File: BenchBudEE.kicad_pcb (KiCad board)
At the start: 2 copper layers, 0 parts

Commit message: 4.18 Initial board layout and design rules mods
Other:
- board outline added: 165.1 x 63.5 mm
- copper layers 2 -> 4
- rule trace_min: 0.254 -> 0.1524
- rule via_min_drill: 0.508 -> 0.3302
- rule via_min_size: 0.889 -> 0.508
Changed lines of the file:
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@@
-(kicad_pcb (version 3) (host pcbnew "(2013-mar-13)-testing")
+(kicad_pcb (version 3) (host pcbnew "(2013-07-07 BZR 4022)-stable")
   (general
     (links 0)
@@
     (area 0 0 0 0)
     (thickness 1.6)
-    (drawings 0)
+    (drawings 4)
     (tracks 0)
     (zones 0)
@@
   (layers
     (15 F.Cu signal)
+    (2 PWR power)
+    (1 GND power)
     (0 B.Cu signal)
     (16 B.Adhes user)
@@
     (22 B.Mask user)
     (23 F.Mask user)
-    (24 Dwgs.User user)
-    (25 Cmts.User user)
-    (26 Eco1.User user)
-    (27 Eco2.User user)
     (28 Edge.Cuts user)
   )
   (setup
     (last_trace_width 0.254)
+    (user_trace_width 0.1524)
     (trace_clearance 0.254)
     (zone_clearance 0.508)
     (zone_45_only no)
-    (trace_min 0.254)
+    (trace_min 0.1524)
     (segment_width 0.2)
     (edge_width 0.1)
     (via_size 0.889)
     (via_drill 0.635)
-    (via_min_size 0.889)
-    (via_min_drill 0.508)
+    (via_min_size 0.508)
+    (via_min_drill 0.3302)
+    (user_via 0.508 0.3302)
     (uvia_size 0.508)
     (uvia_drill 0.127)
     (uvias_allowed no)
-    (uvia_min_size 0.508)
+    (uvia_min_size 0.381)
     (uvia_min_drill 0.127)
     (pcb_text_width 0.3)
@@
     (pad_to_mask_clearance 0)
     (aux_axis_origin 0 0)
-    (visible_elements FFFFFF7F)
+    (visible_elements 7FFFFFFF)
     (pcbplotparams
       (layerselection 3178497)
@@
     (add_net "")
   )
+  (gr_line (start 67.31 67.183) (end 67.31 130.683) (angle 90) (layer Edge.Cuts) (width 0.1))
+  (gr_line (start 232.41 67.183) (end 67.31 67.183) (angle 90) (layer Edge.Cuts) (width 0.1))
+  (gr_line (start 232.41 130.683) (end 232.41 67.183) (angle 90) (layer Edge.Cuts) (width 0.1))
+  (gr_line (start 67.31 130.683) (end 232.41 130.683) (angle 90) (layer Edge.Cuts) (width 0.1))
 )

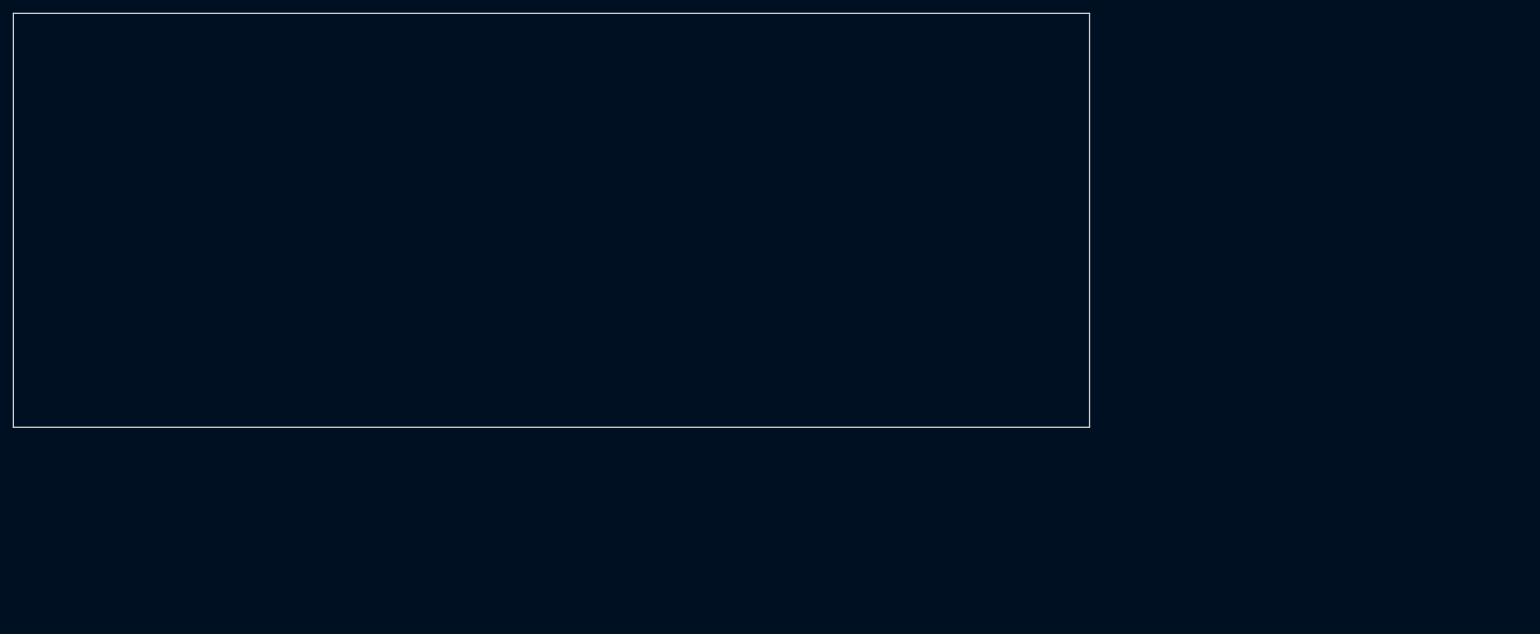
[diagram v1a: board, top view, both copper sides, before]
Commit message: 4.18 Video 2 Changed design rules for pin spacing
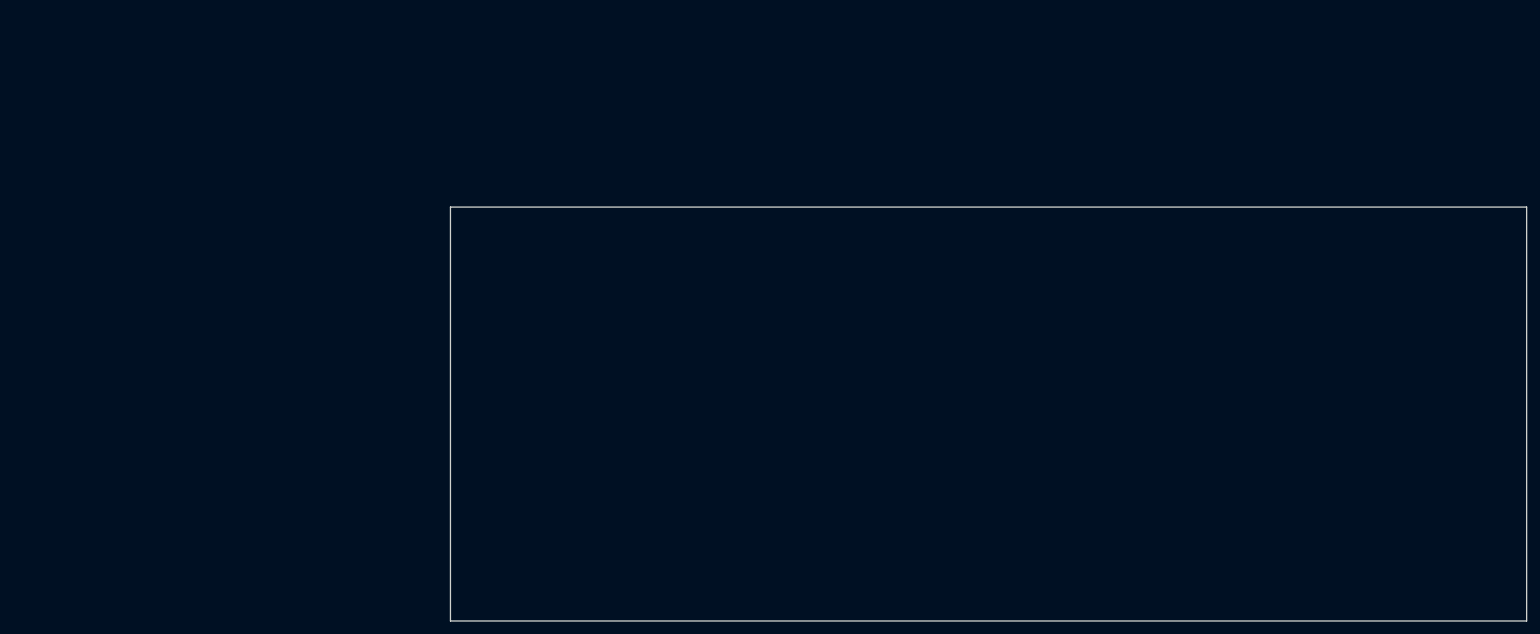
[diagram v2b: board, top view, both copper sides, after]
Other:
- rule pad_to_mask_clearance: 0 -> 0.254
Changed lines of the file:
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@@
     (links 0)
     (no_connects 0)
-    (area 0 0 0 0)
+    (area 104.597999 104.470999 269.798001 168.071001)
     (thickness 1.6)
     (drawings 4)
@@
     (nets 1)
   )
-  (page A4)
+  (page USLedger)
+  (title_block
+    (title BenchBudEE)
+    (rev A)
+    (company "Contextual Electronics")
+  )
   (layers
     (15 F.Cu signal)
@@
     (pad_size 1.5 1.5)
     (pad_drill 0.6)
-    (pad_to_mask_clearance 0)
+    (pad_to_mask_clearance 0.254)
+    (solder_mask_min_width 0.127)
     (aux_axis_origin 0 0)
     (visible_elements 7FFFFFFF)
@@
     (add_net "")
   )
-  (gr_line (start 67.31 67.183) (end 67.31 130.683) (angle 90) (layer Edge.Cuts) (width 0.1))
-  (gr_line (start 232.41 67.183) (end 67.31 67.183) (angle 90) (layer Edge.Cuts) (width 0.1))
-  (gr_line (start 232.41 130.683) (end 232.41 67.183) (angle 90) (layer Edge.Cuts) (width 0.1))
-  (gr_line (start 67.31 130.683) (end 232.41 130.683) (angle 90) (layer Edge.Cuts) (width 0.1))
+  (gr_line (start 134.366 96.901) (end 134.366 160.401) (angle 90) (layer Edge.Cuts) (width 0.1))
+  (gr_line (start 299.466 96.901) (end 134.366 96.901) (angle 90) (layer Edge.Cuts) (width 0.1))
+  (gr_line (start 299.466 160.401) (end 299.466 96.901) (angle 90) (layer Edge.Cuts) (width 0.1))
+  (gr_line (start 134.366 160.401) (end 299.466 160.401) (angle 90) (layer Edge.Cuts) (width 0.1))
 )

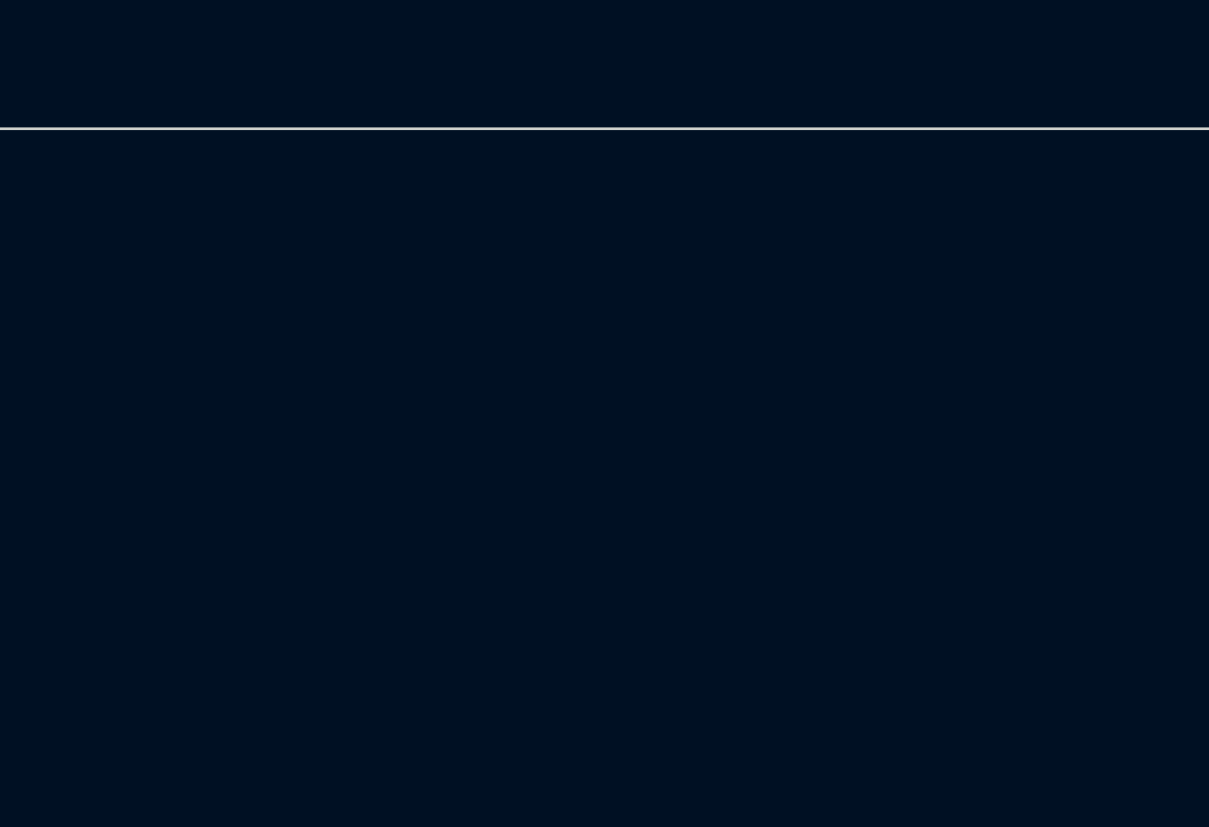
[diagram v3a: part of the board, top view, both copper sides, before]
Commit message: 5.3 Video 2/2 Associating and Placing the Relay Module
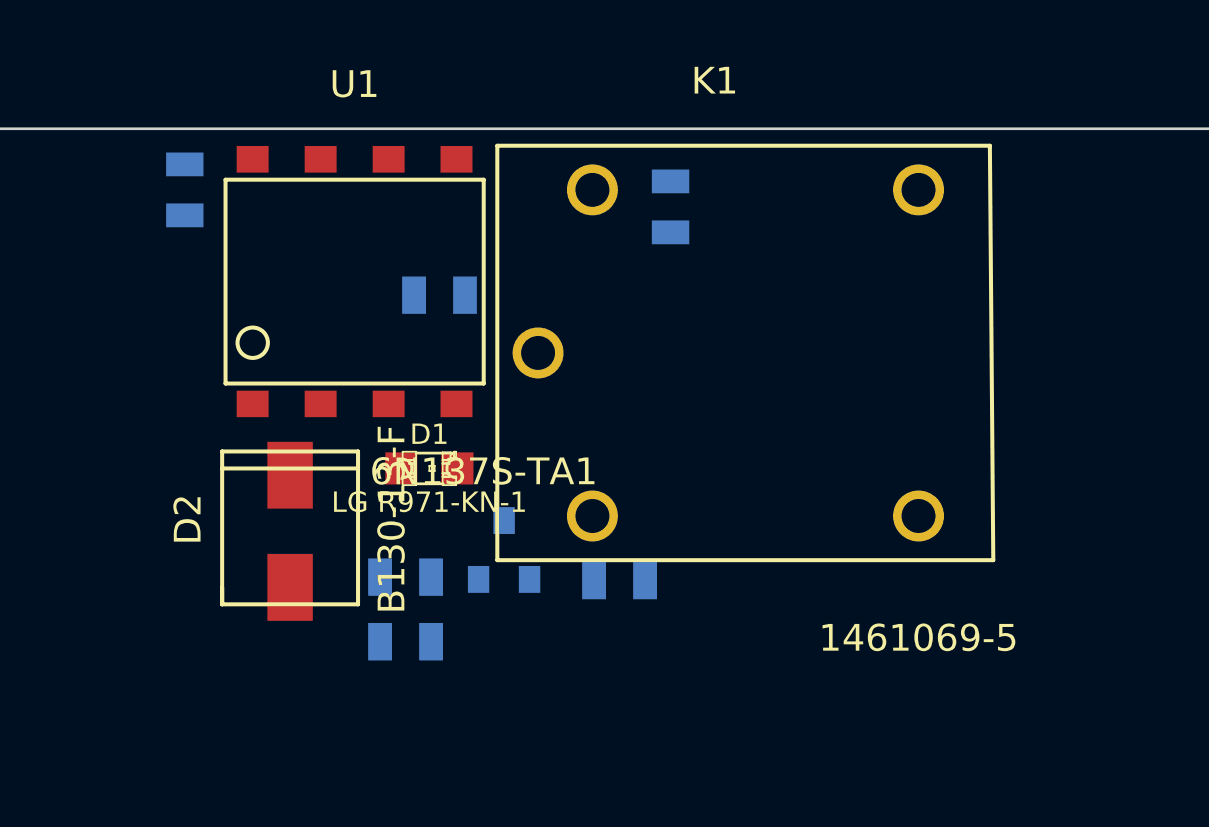
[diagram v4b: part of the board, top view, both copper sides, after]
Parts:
- added D1: LG R971-KN-1, LED-0805, F.Cu at (265.4, 109.6)
- added D2: B130-13-F, SMA, F.Cu at (260.2, 114.0)
- added K1: 1461069-5, TE-SPDT, F.Cu at (271.5, 111.4)
- added Q1: 1461069-5, SOT23, B.Cu at (268.2, 112.6)
- added R1: 500, SM0805, B.Cu at (256.3, 99.2)
- added R2: 200, SM0805, B.Cu at (264.5, 113.7)
- added R3: 100, SM0805, B.Cu at (272.5, 113.8)
- added R4: 0, SM0805, B.Cu at (265.8, 103.1)
- added R5: 0, SM0805, B.Cu at (264.5, 116.1)
- added R6: 0, SM0805, B.Cu at (274.4, 99.8)
- added U1: 6N137S-TA1, 8-SMD, F.Cu at (258.8, 107.2)

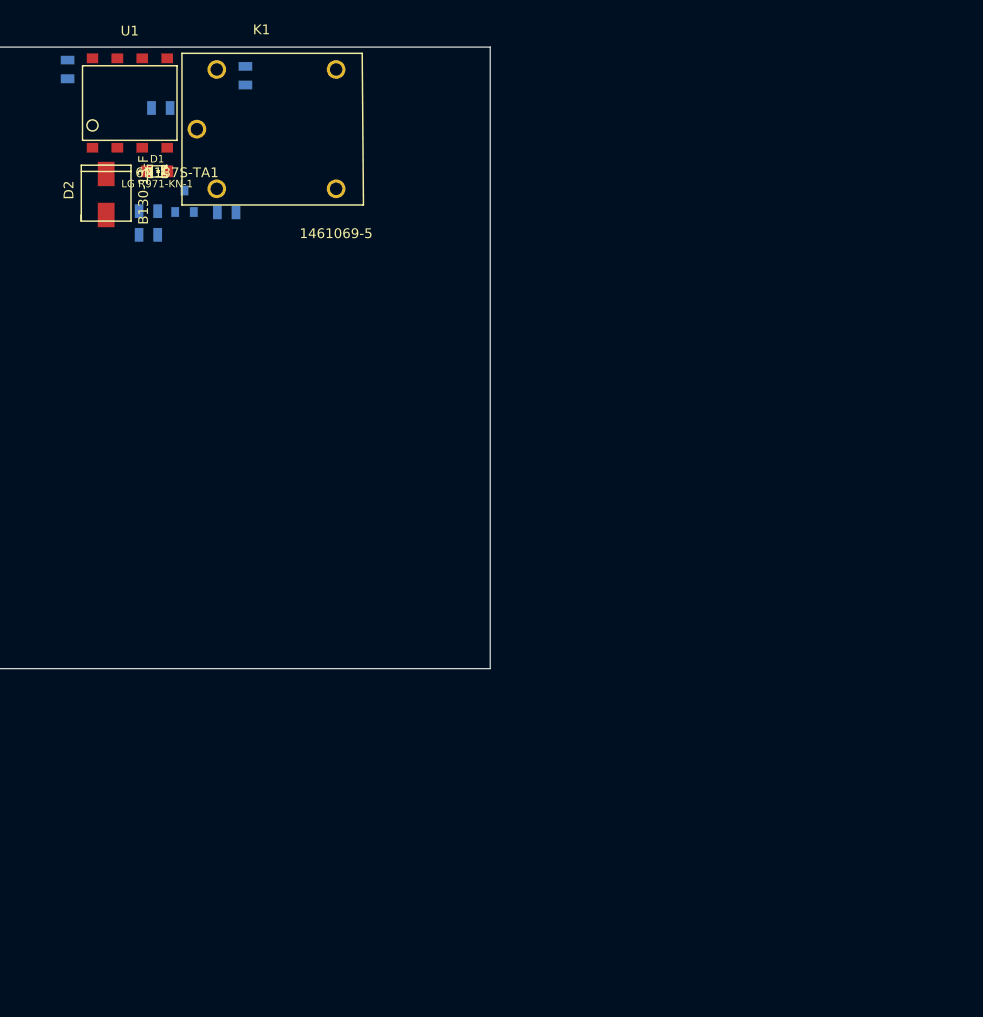
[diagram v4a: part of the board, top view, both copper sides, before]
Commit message: 5.4 Video 1/2 Associating and Placing the Thermocouple Module
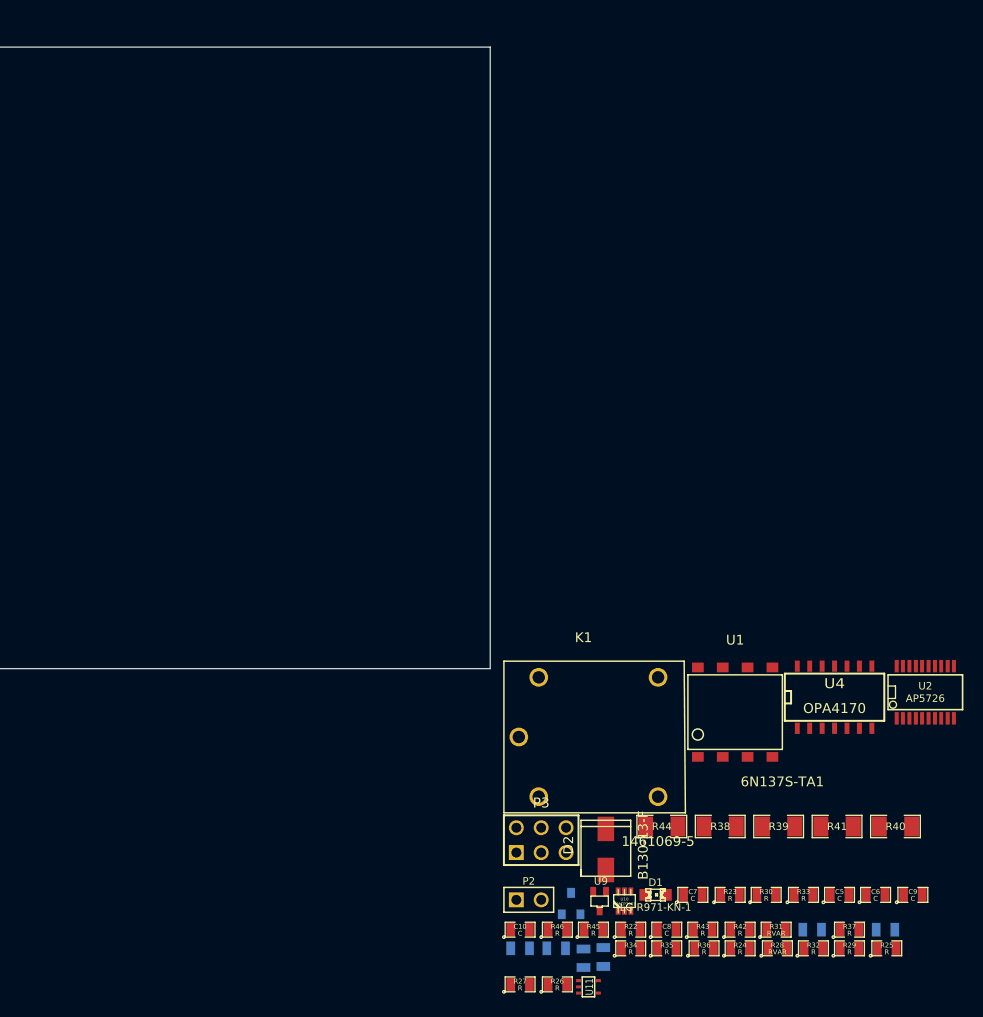
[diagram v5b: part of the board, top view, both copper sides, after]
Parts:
- added C10: C, SM0805, F.Cu at (302.5, 187.1)
- added C5: C, SM0805, F.Cu at (335.2, 183.5)
- added C6: C, SM0805, F.Cu at (338.8, 183.5)
- added C7: C, SM0805, F.Cu at (320.2, 183.5)
- added C8: C, SM0805, F.Cu at (317.5, 187.1)
- added C9: C, SM0805, F.Cu at (342.6, 183.5)
- added P2: CONN_2, PIN_ARRAY_2X1, F.Cu at (303.4, 184.0)
- added P3: CONN_3X2, pin_array_3x2, F.Cu at (304.7, 177.9)
- added R22: R, SM0805, F.Cu at (313.8, 187.1)
- added R23: R, SM0805, F.Cu at (324.0, 183.5)
- added R24: R, SM0805, F.Cu at (325.0, 189.0)
- added R25: R, SM0805, F.Cu at (340.0, 189.0)
- added R26: R, SM0805, F.Cu at (306.3, 192.7)
- added R27: R, SM0805, F.Cu at (302.5, 192.7)
- added R28: RVAR, SM0805, F.Cu at (328.8, 189.0)
- added R29: R, SM0805, F.Cu at (336.2, 189.0)
- added R30: R, SM0805, F.Cu at (327.7, 183.5)
- added R31: RVAR, SM0805, F.Cu at (328.7, 187.1)
- added R32: R, SM0805, F.Cu at (332.5, 189.0)
- added R33: R, SM0805, F.Cu at (331.5, 183.5)
- added R34: R, SM0805, F.Cu at (313.8, 189.0)
- added R35: R, SM0805, F.Cu at (317.5, 189.0)
- added R36: R, SM0805, F.Cu at (321.3, 189.0)
- added R37: R, SM0805, F.Cu at (336.2, 187.1)
- added R38: R, SM1206, F.Cu at (323.0, 176.5)
- added R39: R, SM1206, F.Cu at (328.9, 176.5)
- added R40: R, SM1206, F.Cu at (340.9, 176.5)
- added R41: R, SM1206, F.Cu at (334.9, 176.5)
- added R42: R, SM0805, F.Cu at (325.0, 187.1)
- added R43: R, SM0805, F.Cu at (321.2, 187.1)
- added R44: R, SM1206, F.Cu at (317.0, 176.5)
- added R45: R, SM0805, F.Cu at (310.0, 187.1)
- added R46: R, SM0805, F.Cu at (306.3, 187.1)
- added U10: MCP3901, sot323-6, F.Cu at (313.2, 184.2)
- added U11: LMT84, SOT353, F.Cu at (309.5, 192.9)
- added U2: AP5726, SSOP20, F.Cu at (343.9, 162.8)
- added U4: OPA4170, SO14N, F.Cu at (334.6, 163.2)
- added U9: LM324, SOT323, F.Cu at (310.6, 184.2)
- moved R1 105.0 mm to (309.0, 190.0)
- moved R3 99.5 mm to (339.9, 187.1)
- moved R5 98.2 mm to (332.4, 187.1)
- moved R6 97.2 mm to (311.0, 189.9)
- moved R4 94.9 mm to (306.2, 189.0)
- moved D1 89.8 mm to (316.4, 183.5)
- moved U1 87.7 mm to (320.7, 169.4)
- moved R2 84.3 mm to (302.5, 189.0)
- moved D2 84.2 mm to (311.3, 181.0)
- moved Q1 81.9 mm to (307.7, 184.4)
- moved K1 70.3 mm to (304.4, 173.5)
